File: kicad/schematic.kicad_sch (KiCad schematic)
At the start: 26 parts, among them J1 16X02 LCD Display I2C, J2 500g. Load Cell Sensor, J3 NAU7802, 24-Bit Dual-Channel.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, J4 TP4056 Lithium Battery Chargi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, J5 Soft Power Switch: SPX-17870, Q1 PN2222A, SW1 Tare, SW2 Power, SW3 Up, SW4 Down, SW5 Enter, SW6 Cancel, SW7 Coffee, U1 Step-up DC-to-DC 0.9-5V to 5V

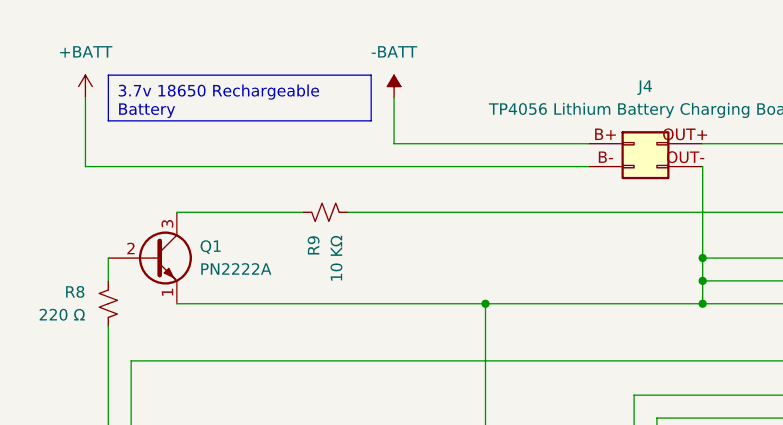
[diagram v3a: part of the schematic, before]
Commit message: add fuse on schematic
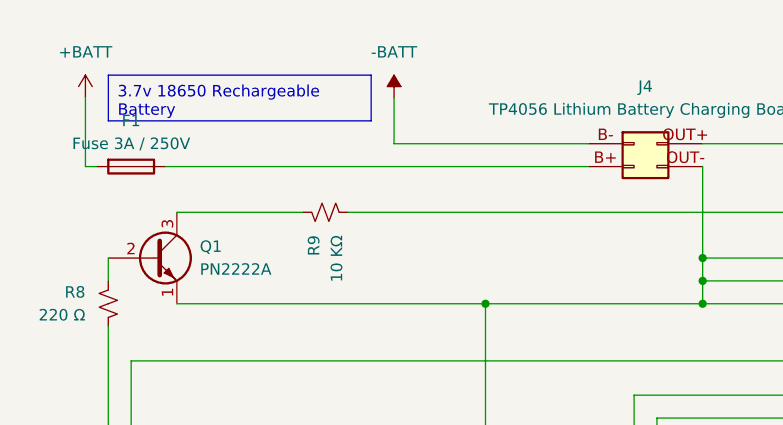
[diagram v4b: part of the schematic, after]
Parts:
- added F1: Fuse 3A / 250V, symbol Device:Fuse
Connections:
- net +BATT: now also F1.2; no longer J4.B- (Pin_2)
- net -BATT: now also J4.B- (1); no longer J4.B+ (1)
- new net: F1.1, J4.B+ (Pin_2)
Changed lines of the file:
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@@
     (stroke (width 0) (type default))
   )
-  (wire (pts (xy 24.13 30.48) (xy 80.01 30.48))
+  (wire (pts (xy 24.13 30.48) (xy 25.4 30.48))
     (stroke (width 0) (type default))
   )
@@
   )
   (wire (pts (xy 135.89 132.08) (xy 137.16 132.08))
+    (stroke (width 0) (type default))
+  )
+  (wire (pts (xy 33.02 30.48) (xy 80.01 30.48))
     (stroke (width 0) (type default))
   )
@@
         )
       )
+    )
+  )
+  (symbol (lib_id "Device:Fuse") (at 29.21 30.48 270) (unit 1)
+    (in_bom yes) (on_board yes) (dnp no) (fields_autoplaced)
+    (property "Reference" "F1" (at 29.21 25.4 90)
+      (effects (font (size 1.27 1.27)))
+    )
+    (property "Value" "Fuse 3A / 250V" (at 29.21 27.94 90)
+      (effects (font (size 1.27 1.27)))
+    )
+    (property "Footprint" "" (at 29.21 28.702 90)
+      (effects (font (size 1.27 1.27)) hide)
+    )
+    (property "Datasheet" "~" (at 29.21 30.48 0)
+      (effects (font (size 1.27 1.27)) hide)
+    )
+    (pin "1")
+    (pin "2")
+    (instances
+      (project "schematic"
+        (path "/85a9fe5f-57a4-44d2-ac06-45fdef87bea2"
+          (reference "F1") (unit 1)
+        )
+      )

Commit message: add IR pump control
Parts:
- added EK8477: 38khz Ir Transmitter, symbol Connector_Generic:Conn_01x03
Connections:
- net at J3.3V (Pin_7), RPPW1.36 (3V3), SW1.3 (B)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: now also EK8477.VCC (Pin_1)
- net at R7.2, SW7.1 (A), SW7.2 (A): now also RPPW1.29 (GPIO22); no longer RPPW1.28 (GND)
- net at RPPW1.7 (GPIO5): now also EK8477.DAT
- net at RPPW1.8 (GND): now also EK8477.GND (Pin_3)
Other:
- moved on the sheet: J2
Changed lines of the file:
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@@
   (title_block
     (title "RPi Pico W - Smart Espresso Scale")
-    (date "2024-02-17")
-    (rev "1.0.0")
+    (date "2024-05-01")
+    (rev "1.1.0")
     (company "Antonios Karagiannis")
   )
@@
   (junction (at 228.6 118.11) (diameter 0) (color 0 0 0 0)
   )
+  (junction (at 81.28 63.5) (diameter 0) (color 0 0 0 0)
+  )
   (junction (at 233.68 153.67) (diameter 0) (color 0 0 0 0)
   )
@@
     (stroke (width 0) (type default))
   )
-  (wire (pts (xy 43.18 80.01) (xy 55.88 80.01))
+  (wire (pts (xy 35.56 80.01) (xy 55.88 80.01))
     (stroke (width 0) (type default))
   )
@@
     (stroke (width 0) (type default))
   )
-  (wire (pts (xy 241.3 105.41) (xy 241.3 132.08))
+  (wire (pts (xy 241.3 102.87) (xy 241.3 132.08))
     (stroke (width 0) (type default))
   )
@@
     (stroke (width 0) (type default))
   )
-  (wire (pts (xy 72.39 102.87) (xy 72.39 107.95))
+  (wire (pts (xy 67.31 111.76) (xy 67.31 115.57))
     (stroke (width 0) (type default))
   )
@@
     (stroke (width 0) (type default))
   )
-  (wire (pts (xy 81.28 97.79) (xy 81.28 110.49))
+  (wire (pts (xy 73.66 106.68) (xy 73.66 118.11))
     (stroke (width 0) (type default))
   )
@@
     (stroke (width 0) (type default))
   )
+  (wire (pts (xy 81.28 63.5) (xy 158.75 63.5))
+    (stroke (width 0) (type default))
+  )
   (wire (pts (xy 129.54 20.32) (xy 134.62 20.32))
     (stroke (width 0) (type default))
@@
     (stroke (width 0) (type default))
   )
-  (wire (pts (xy 72.39 97.79) (xy 81.28 97.79))
-    (stroke (width 0) (type default))
-  )
-  (wire (pts (xy 45.72 102.87) (xy 45.72 82.55))
+  (wire (pts (xy 67.31 106.68) (xy 73.66 106.68))
+    (stroke (width 0) (type default))
+  )
+  (wire (pts (xy 38.1 111.76) (xy 38.1 82.55))
     (stroke (width 0) (type default))
   )
@@
     (stroke (width 0) (type default))
   )
-  (wire (pts (xy 49.53 97.79) (xy 49.53 85.09))
+  (wire (pts (xy 41.91 106.68) (xy 41.91 85.09))
     (stroke (width 0) (type default))
   )
@@
     (stroke (width 0) (type default))
   )
-  (wire (pts (xy 43.18 107.95) (xy 43.18 80.01))
+  (wire (pts (xy 35.56 115.57) (xy 35.56 80.01))
     (stroke (width 0) (type default))
   )
@@
     (stroke (width 0) (type default))
   )
-  (wire (pts (xy 76.2 63.5) (xy 158.75 63.5))
+  (wire (pts (xy 76.2 63.5) (xy 81.28 63.5))
     (stroke (width 0) (type default))
   )
@@
     (stroke (width 0) (type default))
   )
-  (wire (pts (xy 72.39 107.95) (xy 43.18 107.95))
+  (wire (pts (xy 67.31 115.57) (xy 35.56 115.57))
     (stroke (width 0) (type default))
   )
@@
     (stroke (width 0) (type default))
   )
-  (wire (pts (xy 130.81 105.41) (xy 241.3 105.41))
-    (stroke (width 0) (type default))
-  )
   (wire (pts (xy 241.3 132.08) (xy 241.3 144.78))
     (stroke (width 0) (type default))
@@
     (stroke (width 0) (type default))
   )
+  (wire (pts (xy 81.28 87.63) (xy 81.28 63.5))
+    (stroke (width 0) (type default))
+  )
   (wire (pts (xy 190.5 113.03) (xy 190.5 132.08))
     (stroke (width 0) (type default))
@@
     (stroke (width 0) (type default))
   )
-  (wire (pts (xy 45.72 82.55) (xy 55.88 82.55))
-    (stroke (width 0) (type default))
-  )
-  (wire (pts (xy 81.28 110.49) (xy 39.37 110.49))
+  (wire (pts (xy 38.1 82.55) (xy 55.88 82.55))
+    (stroke (width 0) (type default))
+  )
+  (wire (pts (xy 73.66 118.11) (xy 31.75 118.11))
     (stroke (width 0) (type default))
   )
@@
     (stroke (width 0) (type default))
   )
+  (wire (pts (xy 80.01 92.71) (xy 95.25 92.71))
+    (stroke (width 0) (type default))
+  )
   (wire (pts (xy 171.45 27.94) (xy 175.26 27.94))
     (stroke (width 0) (type default))
@@
     (stroke (width 0) (type default))
   )
-  (wire (pts (xy 53.34 97.79) (xy 49.53 97.79))
-    (stroke (width 0) (type default))
-  )
-  (wire (pts (xy 39.37 110.49) (xy 39.37 77.47))
+  (wire (pts (xy 48.26 106.68) (xy 41.91 106.68))
+    (stroke (width 0) (type default))
+  )
+  (wire (pts (xy 31.75 118.11) (xy 31.75 77.47))
     (stroke (width 0) (type default))
   )
@@
     (stroke (width 0) (type default))
   )
-  (wire (pts (xy 39.37 77.47) (xy 55.88 77.47))
+  (wire (pts (xy 31.75 77.47) (xy 55.88 77.47))
     (stroke (width 0) (type default))
   )
@@
     (stroke (width 0) (type default))
   )
-  (wire (pts (xy 53.34 102.87) (xy 45.72 102.87))
+  (wire (pts (xy 130.81 102.87) (xy 241.3 102.87))
+    (stroke (width 0) (type default))
+  )
+  (wire (pts (xy 48.26 111.76) (xy 38.1 111.76))
     (stroke (width 0) (type default))
   )
@@
     (stroke (width 0) (type default))
   )
+  (wire (pts (xy 80.01 90.17) (xy 95.25 90.17))
+    (stroke (width 0) (type default))
+  )
   (wire (pts (xy 137.16 123.19) (xy 130.81 123.19))
     (stroke (width 0) (type default))
@@
     (stroke (width 0) (type default))
   )
-  (wire (pts (xy 49.53 85.09) (xy 55.88 85.09))
+  (wire (pts (xy 41.91 85.09) (xy 55.88 85.09))
     (stroke (width 0) (type default))
   )
@@
   )
   (wire (pts (xy 121.92 20.32) (xy 116.84 20.32))
+    (stroke (width 0) (type default))
+  )
+  (wire (pts (xy 80.01 87.63) (xy 81.28 87.63))
     (stroke (width 0) (type default))
   )
@@
     )
   )
+  (symbol (lib_id "Connector_Generic:Conn_01x03") (at 74.93 90.17 0) (mirror y) (unit 1)
+    (in_bom yes) (on_board yes) (dnp no)
+    (property "Reference" "EK8477" (at 72.39 88.9 0)
+      (effects (font (size 1.27 1.27)) (justify left))
+    )
+    (property "Value" "38khz Ir Transmitter" (at 72.39 91.44 0)
+      (effects (font (size 1.27 1.27)) (justify left))
+    )
+    (property "Footprint" "" (at 74.93 90.17 0)
+      (effects (font (size 1.27 1.27)) hide)
+    )
+    (property "Datasheet" "~" (at 74.93 90.17 0)
+      (effects (font (size 1.27 1.27)) hide)
+    )
+    (pin "VCC")
+    (pin "GND")
+    (pin "DAT")
+    (instances
+      (project "schematic"
+        (path "/85a9fe5f-57a4-44d2-ac06-45fdef87bea2"
+          (reference "EK8477") (unit 1)
+        )
+      )
+    )
+  )
   (symbol (lib_id "Switch:SW_MEC_5G") (at 195.58 144.78 0) (unit 1)
     (in_bom yes) (on_board yes) (dnp no) (fields_autoplaced)
@@
     )
   )
-  (symbol (lib_id "Connector_Generic:Conn_02x02_Counter_Clockwise") (at 58.42 95.25 0) (unit 1)
+  (symbol (lib_id "Connector_Generic:Conn_02x02_Counter_Clockwise") (at 53.34 104.14 0) (unit 1)
     (in_bom yes) (on_board yes) (dnp no) (fields_autoplaced)
-    (property "Reference" "J2" (at 59.69 88.9 0)
-      (effects (font (size 1.27 1.27)))
-    )
-    (property "Value" "500g. Load Cell Sensor" (at 59.69 91.44 0)
-      (effects (font (size 1.27 1.27)))
-    )
-    (property "Footprint" "" (at 58.42 95.25 0)
-      (effects (font (size 1.27 1.27)) hide)
-    )
-    (property "Datasheet" "~" (at 58.42 95.25 0)
-      (effects (font (size 1.27 1.27)) hide)
-    )
+    (property "Reference" "J2" (at 54.61 97.79 0)
+      (effects (font (size 1.27 1.27)))
+    )
+    (property "Value" "500g. Load Cell Sensor" (at 54.61 100.33 0)
+      (effects (font (size 1.27 1.27)))
+    )
+    (property "Footprint" "" (at 53.34 104.14 0)
+      (effects (font (size 1.27 1.27)) hide)
+    )
+    (property "Datasheet" "~" (at 53.34 104.14 0)
+      (effects (font (size 1.27 1.27)) hide)
+    )
